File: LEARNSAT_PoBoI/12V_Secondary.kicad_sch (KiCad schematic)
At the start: 17 parts, among them Q12 SI5418DU-T1-GE3, Q3 SI7164DP-T1-GE3, U13 INA219AIDCNR, U18 LTC4231IUD-2#TRPBF

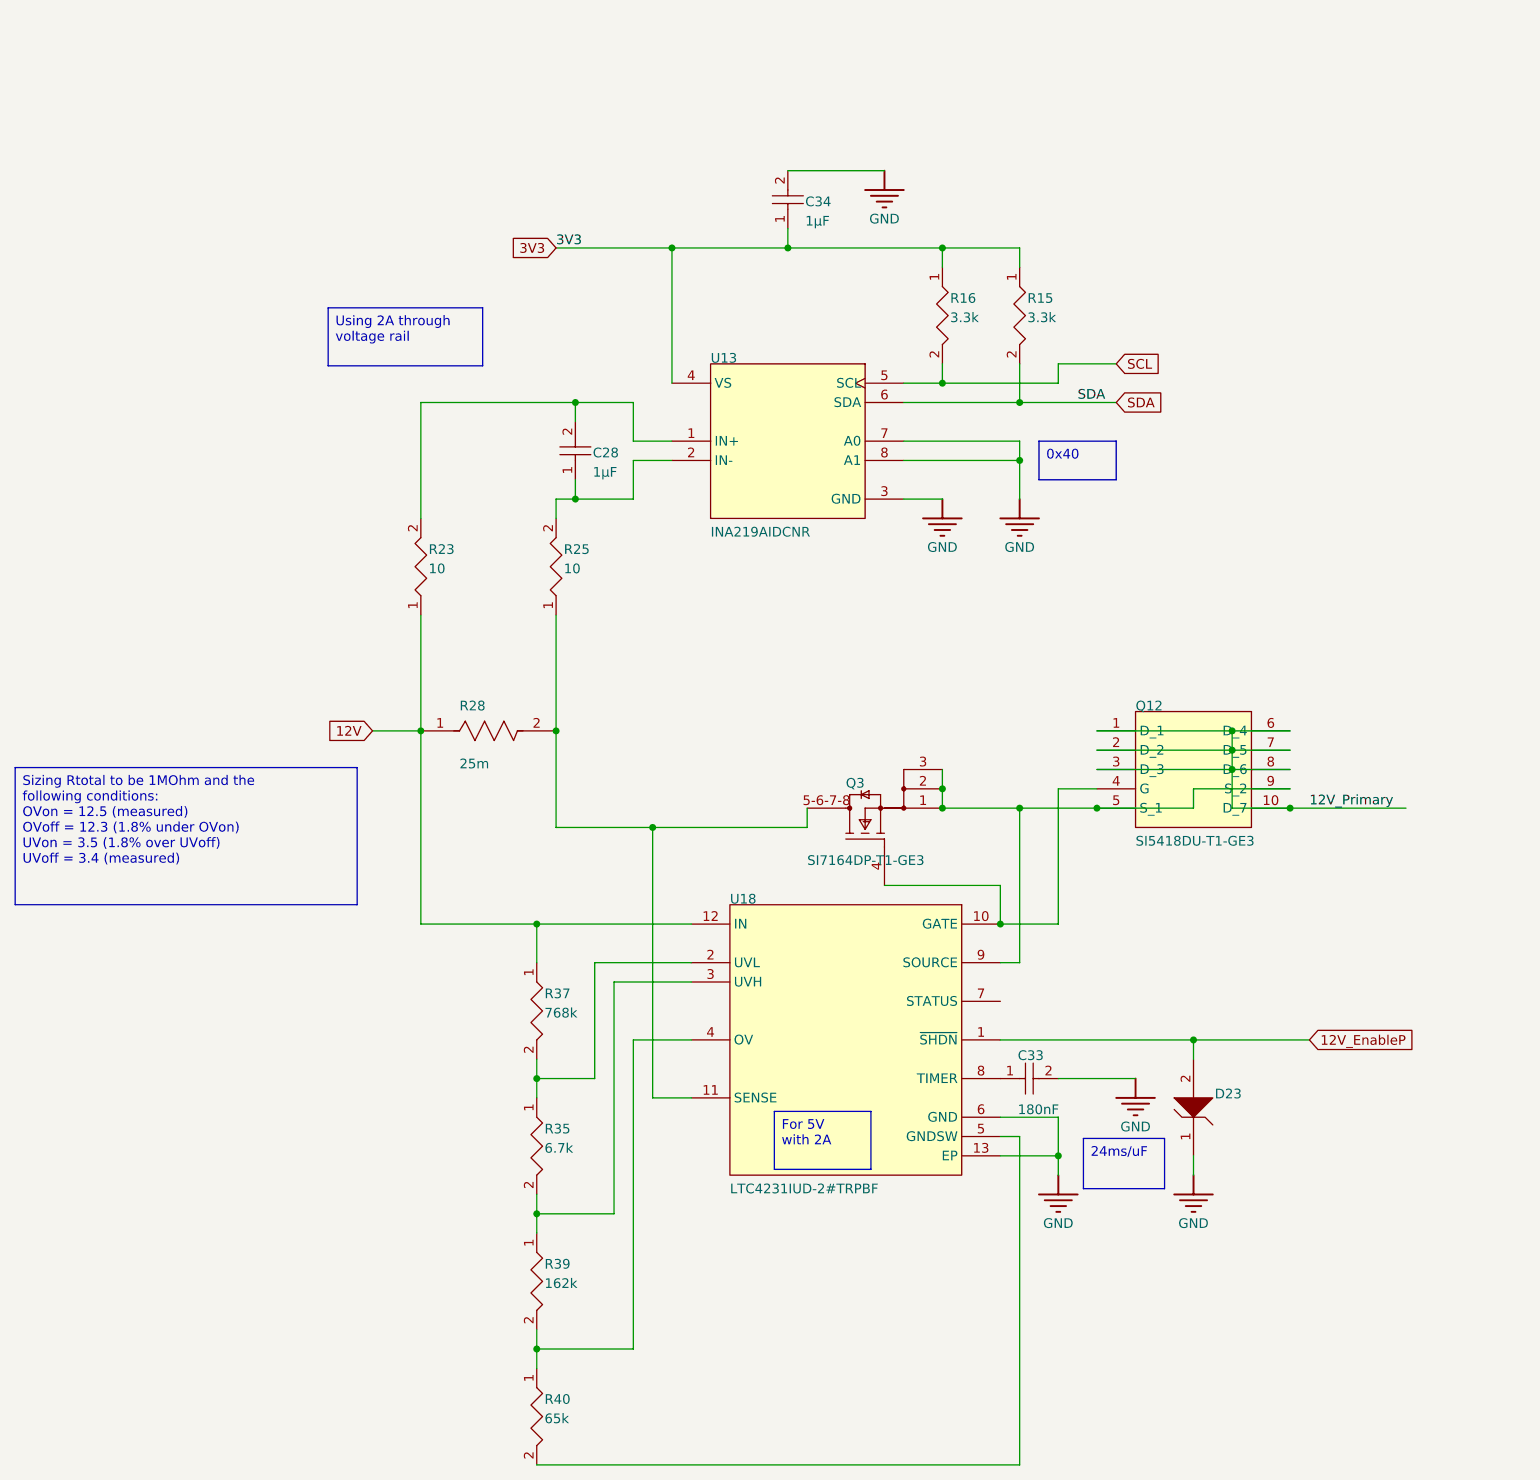
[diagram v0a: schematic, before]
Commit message: Edited 12V Rail schematics
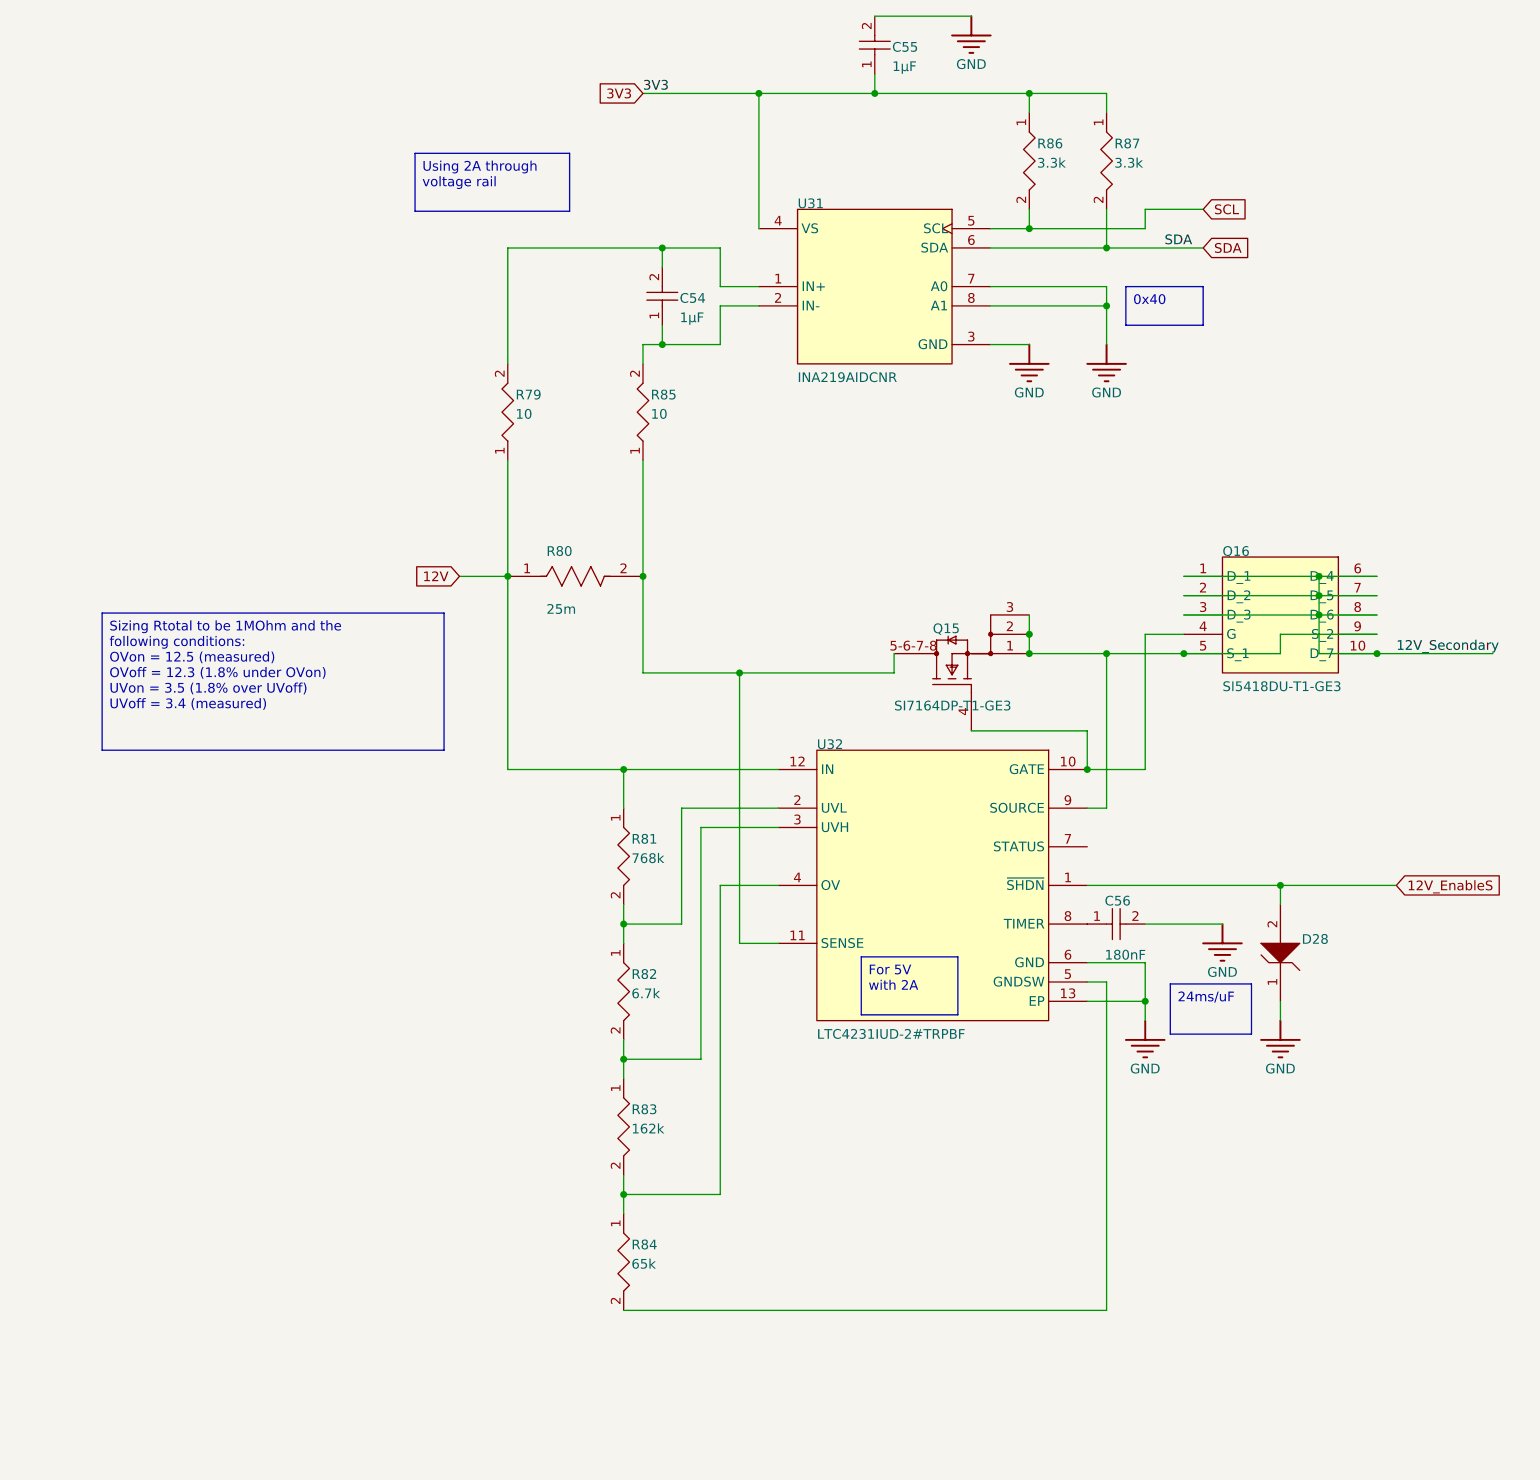
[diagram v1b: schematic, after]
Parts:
- removed C28: Capacitor 1 uF +/- 10% 25 V 0603, Vault:CAPC1608X90X40LL10T20, symbol UGA SSRL Hardware Team:root_1_CAP-NP-2_UGA SSRL Hardware Team
- removed C33: C0805C184K5RACTU, Vault:FP-C0805C-DN-IPC_A, symbol UGA SSRL Hardware Team:root_0_CAP-NP-2_UGA SSRL Hardware Team
- removed C34: Capacitor 1uF +/- 10% 16V 0603, Vault:CAPC1608X90X35ML15T15, symbol UGA SSRL Hardware Team:root_1_CAP-NP-2_UGA SSRL Hardware Team
- removed D23: MM3Z3V6T1G, Vault:ONSC-SOD-323-2-477-02_V, symbol Altium Content Vault:root_3_ONSC-K1A2-2_Altium Content Vault
- removed Q12: SI5418DU-T1-GE3, Vault:SI5418DU-T1-GE3-Footprint-1, symbol UGA SSRL Hardware Team:root_0_SI5418DU-T1-GE3-Symbol-1_UGA SSRL Hardware Team
- removed Q3: SI7164DP-T1-GE3, Vault:Vishay_S17-0173-SINGLE_MFG, symbol UGA SSRL Hardware Team:root_1_SI7164DP-T1-GE3_UGA SSRL Hardware Team
- removed R15, R16: CRCW12103K30JNEA, Vault:FP-CRCW1210-e3-IPC_C, symbol UGA SSRL Hardware Team:root_3_RES-2_UGA SSRL Hardware Team_0
- removed R23, R25: Resistor 10R +/-1 % 0402 63 mW, Vault:RESC0402(1005)_L, symbol UGA SSRL Hardware Team:root_1_RES-2_UGA SSRL Hardware Team_0
- removed R28: CSR1206FK25L0, Vault:FP-CSR1206-IPC_C, symbol Altium Content Vault:root_0_1029c3af85768c4190bb7ad29bc67b5_Altium Content Vault
- removed R35: CRCW12067K50FKEA, Vault:FP-CRCW1206-e3-IPC_A, symbol UGA SSRL Hardware Team:root_3_RES-2_UGA SSRL Hardware Team_0
- removed R37: 768KR2F, Vault:RESC0402(1005)_L, symbol UGA SSRL Hardware Team:root_3_768KR2F_UGA SSRL Hardware Team_0
- removed R39: PTN0603E8002BST1, Vault:FP-PTN0603-IPC_B, symbol UGA SSRL Hardware Team:root_3_RES-2_UGA SSRL Hardware Team_0
- removed R40: RT1206FRE07150KL, Vault:FP-RT1206-IPC_C, symbol UGA SSRL Hardware Team:root_3_RES-2_UGA SSRL Hardware Team_0
- removed U13: INA219AIDCNR, Vault:FP-DCN0008A-IPC_A, symbol UGA SSRL Hardware Team:root_0_e16934b8ef90d0e345b266f0ae9cd81_UGA SSRL Hardware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
- removed U18: LTC4231IUD-2#TRPBF, Vault:FP-UD-12-05-08-1855-IPC_A, symbol UGA SSRL Hardware Team:root_0_94c330ae140e2337d879337fe7aaeec_UGA SSRL Hardware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
- added C54: Capacitor 1 uF +/- 10% 25 V 0603, Vault:CAPC1608X90X40LL10T20, symbol UGA SSRL Hardware Team:root_1_CAP-NP-2_UGA SSRL Hardware Team
- added C55: Capacitor 1uF +/- 10% 16V 0603, Vault:CAPC1608X90X35ML15T15, symbol UGA SSRL Hardware Team:root_1_CAP-NP-2_UGA SSRL Hardware Team
- added C56: C0805C184K5RACTU, Vault:FP-C0805C-DN-IPC_A, symbol UGA SSRL Hardware Team:root_0_CAP-NP-2_UGA SSRL Hardware Team
- added D28: MM3Z3V6T1G, Vault:ONSC-SOD-323-2-477-02_V, symbol Altium Content Vault:root_3_ONSC-K1A2-2_Altium Content Vault
- added Q15: SI7164DP-T1-GE3, Vault:Vishay_S17-0173-SINGLE_MFG, symbol UGA SSRL Hardware Team:root_1_SI7164DP-T1-GE3_UGA SSRL Hardware Team
- added Q16: SI5418DU-T1-GE3, Vault:SI5418DU-T1-GE3-Footprint-1, symbol UGA SSRL Hardware Team:root_0_SI5418DU-T1-GE3-Symbol-1_UGA SSRL Hardware Team
- added R79, R85: Resistor 10R +/-1 % 0402 63 mW, Vault:RESC0402(1005)_L, symbol UGA SSRL Hardware Team:root_1_RES-2_UGA SSRL Hardware Team_0
- added R80: CSR1206FK25L0, Vault:FP-CSR1206-IPC_C, symbol Altium Content Vault:root_0_1029c3af85768c4190bb7ad29bc67b5_Altium Content Vault
- added R81: 768KR2F, Vault:RESC0402(1005)_L, symbol UGA SSRL Hardware Team:root_3_768KR2F_UGA SSRL Hardware Team_0
- added R82: CRCW12067K50FKEA, Vault:FP-CRCW1206-e3-IPC_A, symbol UGA SSRL Hardware Team:root_3_RES-2_UGA SSRL Hardware Team_0
- added R83: PTN0603E8002BST1, Vault:FP-PTN0603-IPC_B, symbol UGA SSRL Hardware Team:root_3_RES-2_UGA SSRL Hardware Team_0
- added R84: RT1206FRE07150KL, Vault:FP-RT1206-IPC_C, symbol UGA SSRL Hardware Team:root_3_RES-2_UGA SSRL Hardware Team_0
- added R86, R87: CRCW12103K30JNEA, Vault:FP-CRCW1210-e3-IPC_C, symbol UGA SSRL Hardware Team:root_3_RES-2_UGA SSRL Hardware Team_0
- added U31: INA219AIDCNR, Vault:FP-DCN0008A-IPC_A, symbol UGA SSRL Hardware Team:root_0_e16934b8ef90d0e345b266f0ae9cd81_UGA SSRL Hardware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
- added U32: LTC4231IUD-2#TRPBF, Vault:FP-UD-12-05-08-1855-IPC_A, symbol UGA SSRL Hardware Team:root_0_94c330ae140e2337d879337fe7aaeec_UGA SSRL Hardware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
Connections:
- net 12V: now also R79.1, R80.1, R81.1, U32.12 (IN)
- net 3V3: now also C55.1, R86.1, R87.1, U31.4 (VS)
- net GND: now also C55.2, C56.2, D28.1 (K), U31.3 (GND), U31.7 (A0), U31.8 (A1), U32.13 (EP), U32.6 (GND)
- net SCL: now also R86.2, U31.5 (SCL)
- net SDA: now also R87.2, U31.6 (SDA)
- new net: C54.2, R79.2, U31.1 (IN+)
- new net: C54.1, R85.2, U31.2 (IN-)
- new net: Q15.5-6-7-8 (D), R80.2, R85.1, U32.11 (SENSE)
- new net: Q15.4 (G), Q16.4 (G), U32.10 (GATE)
- new net: R81.2, R82.1, U32.2 (UVL)
- new net: R82.2, R83.1, U32.3 (UVH)
- new net: R83.2, R84.1, U32.4 (OV)
- new net: R84.2, U32.5 (GNDSW)
- new net: C56.1, U32.8 (TIMER)
- new net: Q15.1 (S), Q15.2 (S), Q15.3 (S), Q16.5 (S_1), Q16.9 (S_2), U32.9 (SOURCE)
- new net 12V_EnableS: D28.2 (A), U32.1 (~{SHDN})
- new net 12V_Secondary: Q16.1 (D_1), Q16.10 (D_7), Q16.2 (D_2), Q16.3 (D_3), Q16.6 (D_4), Q16.7 (D_5), Q16.8 (D_6)
